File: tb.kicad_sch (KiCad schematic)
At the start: 67 parts, among them U4 JHL6340SLLSQ, U5 MX25L8006EM1I-12G, U6 SI52112-B6-GT, U7 MX25L8006EM2I-12G, Y1 ABM8G-25.000MHZ-B4Y-T, Y2 ABM8G-25.000MHZ-B4Y-T

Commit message: [#58582] Globlib
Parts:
- C100, C102, C103, C105, C106, C107, C108, C109, C110, C111, C112, C99: footprint thunderbolt-pcie-adapter-footprints:C_0402_1005Metric -> antmicro-footprints:C_0402_1005Metric; symbol thunderbolt-pcie-adapter:C_220n_0402 -> antmicroCapacitors0402:C_220n_0402
- C101, C104, C115, C98: footprint thunderbolt-pcie-adapter-footprints:C_0402_1005Metric -> antmicro-footprints:C_0402_1005Metric; symbol thunderbolt-pcie-adapter:C_100n_0402 -> antmicroCapacitors0402:C_100n_0402
- C113, C114, C116, C117: footprint thunderbolt-pcie-adapter-footprints:C_0402_1005Metric -> antmicro-footprints:C_0402_1005Metric; symbol thunderbolt-pcie-adapter:C_10p_0402 -> antmicroCapacitors0402:C_10p_0402
- R50, R51, R52, R53: footprint thunderbolt-pcie-adapter-footprints:R_0402_1005Metric -> antmicro-footprints:R_0402_1005Metric; symbol thunderbolt-pcie-adapter:R_3k3_0402 -> antmicroResistors0402:R_3k3_0402
- R54, R55, R70, R71, R82: footprint thunderbolt-pcie-adapter-footprints:R_0402_1005Metric -> antmicro-footprints:R_0402_1005Metric; symbol thunderbolt-pcie-adapter:R_1M_0402 -> antmicroResistors0402:R_1M_0402
- R56, R64, R65, R66, R67, R78, R79, R80, R83, R85: footprint thunderbolt-pcie-adapter-footprints:R_0402_1005Metric -> antmicro-footprints:R_0402_1005Metric; symbol thunderbolt-pcie-adapter:R_10k_0402 -> antmicroResistors0402:R_10k_0402
- R57, R60, R72, R75, R77, R81, R84, R86, R87, R90: footprint thunderbolt-pcie-adapter-footprints:R_0402_1005Metric -> antmicro-footprints:R_0402_1005Metric; symbol thunderbolt-pcie-adapter:R_100k_0402 -> antmicroResistors0402:R_100k_0402
- R58, R59, R61, R62: footprint thunderbolt-pcie-adapter-footprints:R_0402_1005Metric -> antmicro-footprints:R_0402_1005Metric; symbol thunderbolt-pcie-adapter:R_2k2_0402 -> antmicroResistors0402:R_2k2_0402
- R63, R76: footprint thunderbolt-pcie-adapter-footprints:R_0402_1005Metric -> antmicro-footprints:R_0402_1005Metric; symbol thunderbolt-pcie-adapter:R_14k_0402 -> antmicroResistors0402:R_14k_0402
- R68, R73: footprint thunderbolt-pcie-adapter-footprints:R_0402_1005Metric -> antmicro-footprints:R_0402_1005Metric; symbol thunderbolt-pcie-adapter:R_499R_0402 -> antmicroResistors0402:R_499R_0402
- R69: footprint thunderbolt-pcie-adapter-footprints:R_0402_1005Metric -> antmicro-footprints:R_0402_1005Metric; symbol thunderbolt-pcie-adapter:R_4k75_0.5%_0402 -> antmicroResistors0402:R_4k75_0.5%_0402
- R74: footprint thunderbolt-pcie-adapter-footprints:R_0402_1005Metric -> antmicro-footprints:R_0402_1005Metric; symbol thunderbolt-pcie-adapter:R_3k01_0402 -> antmicroResistors0402:R_3k01_0402
- R88, R89: footprint thunderbolt-pcie-adapter-footprints:R_0402_1005Metric -> antmicro-footprints:R_0402_1005Metric; symbol thunderbolt-pcie-adapter:R_100R_0402 -> antmicroResistors0402:R_100R_0402
- U4: footprint thunderbolt-pcie-adapter-footprints:JHL6340SLLSQ -> antmicro-footprints:JHL6340SLLSQ; symbol thunderbolt-pcie-adapter:JHL6340SLLSQ -> antmicroInterfaceControllers:JHL6340SLLSQ
- U5: footprint thunderbolt-pcie-adapter-footprints:SOIC-8_3.9x4.9x1.75mm_P1.27mm -> antmicro-footprints:SOIC-8_3.9x4.9x1.75mm_P1.27mm; symbol thunderbolt-pcie-adapter:MX25L8006EM1I-12G -> antmicroMemory:MX25L8006EM1I-12G
- U6: footprint thunderbolt-pcie-adapter-footprints:TSSOP-8_3x4.4mm_P0.65mm -> antmicro-footprints:TSSOP-8_3x4.4mm_P0.65mm; symbol thunderbolt-pcie-adapter:SI52112-B6-GT -> antmicroClockTimingClockGeneratorsPLLsFrequencySynthesizers:SI52112-B6-GT
- U7: footprint thunderbolt-pcie-adapter-footprints:SOIC-8_5.3x5.3x2mm_P1.27mm -> antmicro-footprints:SOIC-8_5.3x5.3x2mm_P1.27mm; symbol thunderbolt-pcie-adapter:MX25L8006EM2I-12G -> antmicroMemory:MX25L8006EM2I-12G

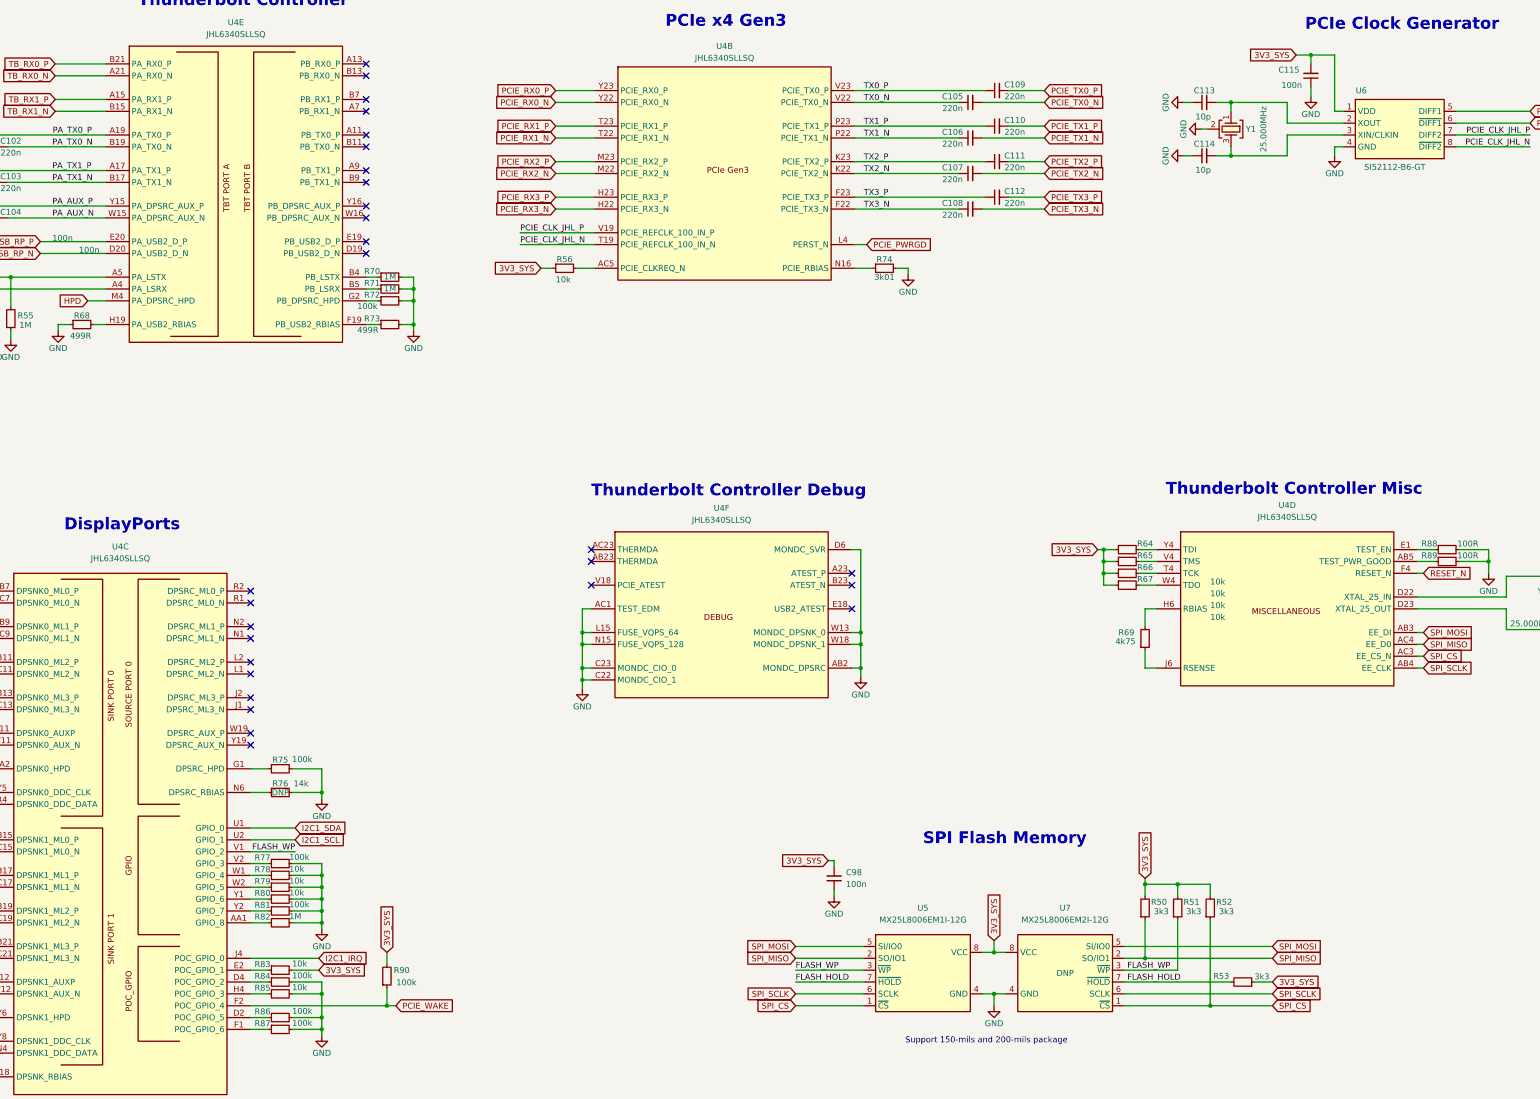
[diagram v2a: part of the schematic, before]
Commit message: [#58582] Update ICs to global libs
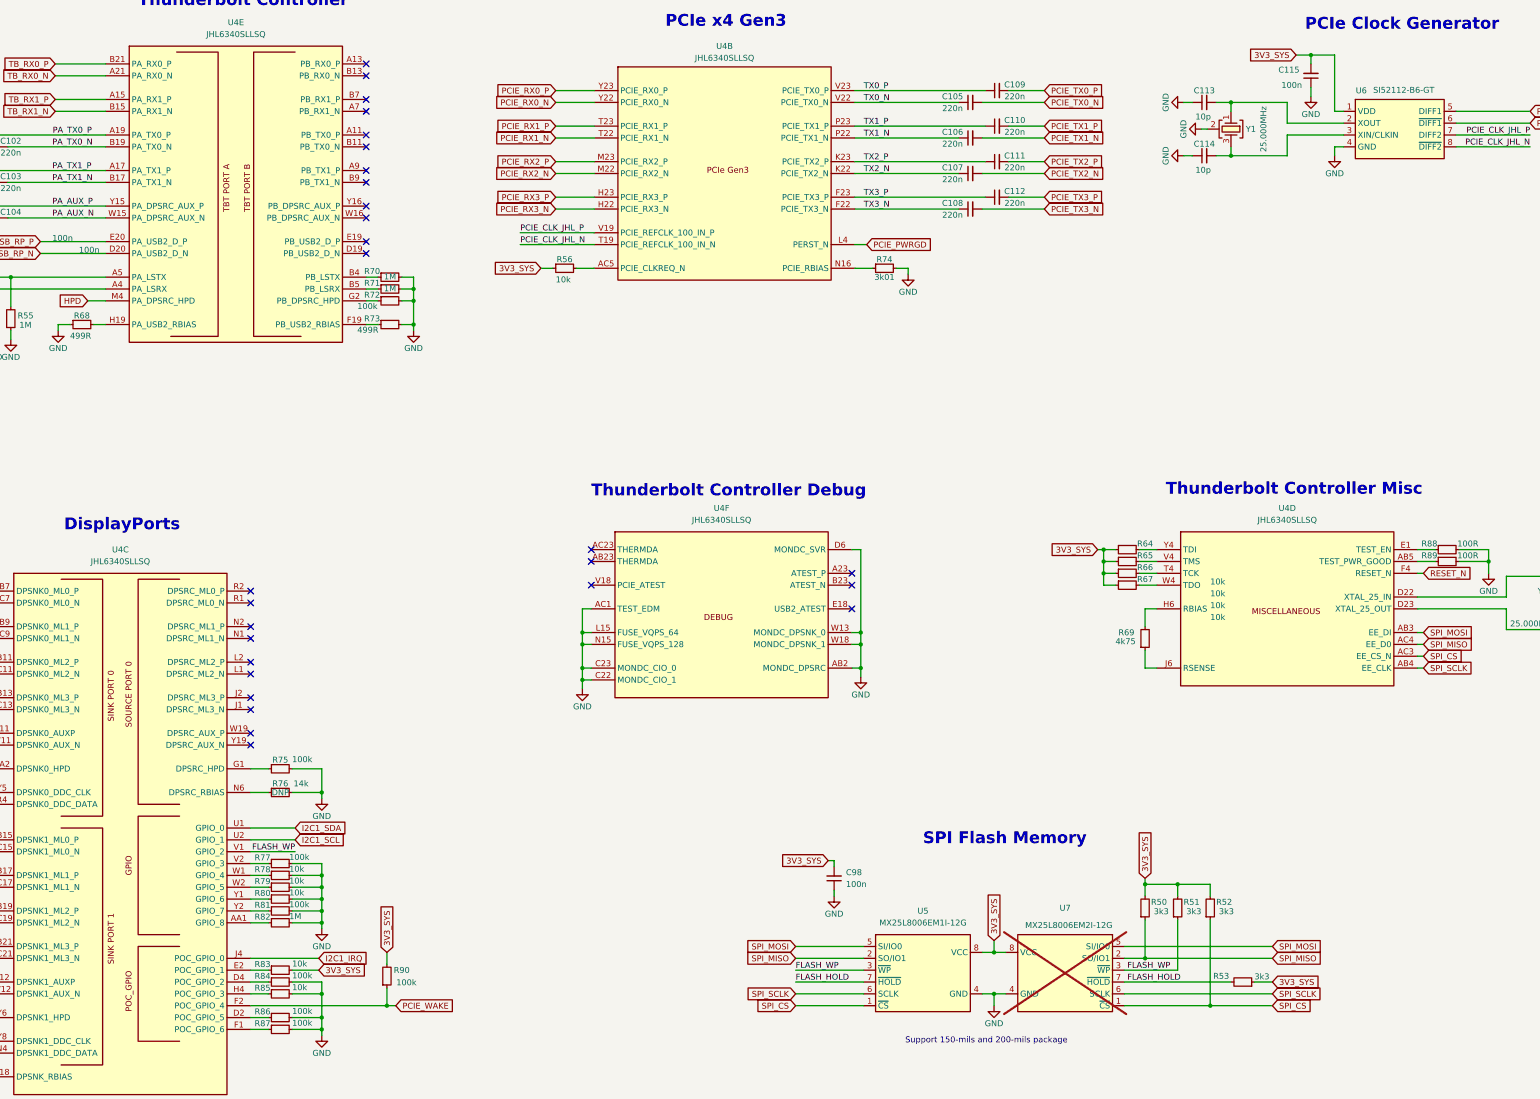
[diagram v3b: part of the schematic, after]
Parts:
- U6: Manufacturer Skyworks -> Skyworks Solutions
- U7: DNP DNP -> (none); now not fitted
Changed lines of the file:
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@@
     )
   )
-  (symbol (lib_name "JHL6340SLLSQ_3") (lib_id "antmicroInterfaceControllers:JHL6340SLLSQ") (at 76.2 40.64 0) (unit 5)
+  (symbol (lib_id "antmicroInterfaceControllers:JHL6340SLLSQ") (at 76.2 40.64 0) (unit 5)
     (in_bom yes) (on_board yes) (dnp no) (fields_autoplaced)
     (property "Reference" "U4" (at 104.14 31.75 0)
@@
   )
   (symbol (lib_id "antmicroMemory:MX25L8006EM2I-12G") (at 294.64 229.87 0) (mirror y) (unit 1)
-    (in_bom yes) (on_board yes) (dnp no)
+    (in_bom yes) (on_board yes) (dnp yes)
     (property "Reference" "U7" (at 281.94 221.615 0)
       (effects (font (size 1.27 1.27) (thickness 0.15)))
     )
-    (property "Value" "MX25L8006EM2I-12G" (at 281.94 224.155 0)
-      (effects (font (size 1.27 1.27) (thickness 0.15)))
+    (property "Value" "MX25L8006EM2I-12G" (at 292.1 226.06 0)
+      (effects (font (size 1.27 1.27) (thickness 0.15)) (justify left bottom))
     )
     (property "Footprint" "antmicro-footprints:SOIC-8_5.3x5.3x2mm_P1.27mm" (at 259.08 234.95 0)
@@
       (effects (font (size 1.27 1.27) (thickness 0.15)) (justify left bottom) hide)
     )
-    (property "DNP" "DNP" (at 281.94 235.585 0)
-      (effects (font (size 1.27 1.27)))
-    )
     (pin "1")
     (pin "2")
@@
   (symbol (lib_id "antmicroMemory:MX25L8006EM1I-12G") (at 238.76 229.87 0) (unit 1)
     (in_bom yes) (on_board yes) (dnp no) (fields_autoplaced)
-    (property "Reference" "U5" (at 251.46 221.615 0)
+    (property "Reference" "U5" (at 251.46 222.25 0)
       (effects (font (size 1.27 1.27) (thickness 0.15)))
     )
-    (property "Value" "MX25L8006EM1I-12G" (at 251.46 224.155 0)
+    (property "Value" "MX25L8006EM1I-12G" (at 251.46 224.79 0)
       (effects (font (size 1.27 1.27) (thickness 0.15)))
     )
@@
       (effects (font (size 1.27 1.27) (thickness 0.15)))
     )
-    (property "Value" "SI52112-B6-GT" (at 346.075 63.5 0)
+    (property "Value" "SI52112-B6-GT" (at 347.98 46.99 0)
       (effects (font (size 1.27 1.27) (thickness 0.15)) (justify left bottom))
     )
@@
       (effects (font (size 1.27 1.27) (thickness 0.15)) (justify left bottom) hide)
     )
-    (property "Manufacturer" "Skyworks" (at 379.73 66.04 0)
+    (property "Manufacturer" "Skyworks Solutions" (at 379.73 66.04 0)
       (effects (font (size 1.27 1.27) (thickness 0.15)) (justify left bottom) hide)
     )
@@
     )
   )
-  (symbol (lib_name "JHL6340SLLSQ_4") (lib_id "antmicroInterfaceControllers:JHL6340SLLSQ") (at 51.435 153.67 0) (unit 3)
+  (symbol (lib_id "antmicroInterfaceControllers:JHL6340SLLSQ") (at 51.435 153.67 0) (unit 3)
     (in_bom yes) (on_board yes) (dnp no) (fields_autoplaced)
-    (property "Reference" "U4" (at 79.375 144.145 0)
+    (property "Reference" "U4" (at 79.375 144.78 0)
       (effects (font (size 1.27 1.27) (thickness 0.15)))
     )
-    (property "Value" "JHL6340SLLSQ" (at 79.375 146.685 0)
+    (property "Value" "JHL6340SLLSQ" (at 79.375 147.32 0)
       (effects (font (size 1.27 1.27) (thickness 0.15)))
     )
@@
     )
   )
-  (symbol (lib_name "JHL6340SLLSQ_2") (lib_id "antmicroInterfaceControllers:JHL6340SLLSQ") (at 180.34 144.78 0) (unit 6)
+  (symbol (lib_id "antmicroInterfaceControllers:JHL6340SLLSQ") (at 180.34 144.78 0) (unit 6)
     (in_bom yes) (on_board yes) (dnp no) (fields_autoplaced)
     (property "Reference" "U4" (at 208.28 135.89 0)
@@
     )
   )
-  (symbol (lib_name "JHL6340SLLSQ_1") (lib_id "antmicroInterfaceControllers:JHL6340SLLSQ") (at 301.625 144.78 0) (unit 4)
+  (symbol (lib_id "antmicroInterfaceControllers:JHL6340SLLSQ") (at 301.625 144.78 0) (unit 4)
     (in_bom yes) (on_board yes) (dnp no) (fields_autoplaced)
-    (property "Reference" "U4" (at 329.565 135.255 0)
+    (property "Reference" "U4" (at 329.565 135.89 0)
       (effects (font (size 1.27 1.27) (thickness 0.15)))
     )
-    (property "Value" "JHL6340SLLSQ" (at 329.565 137.795 0)
+    (property "Value" "JHL6340SLLSQ" (at 329.565 138.43 0)
       (effects (font (size 1.27 1.27) (thickness 0.15)))
     )

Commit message: [#58582] Update GND to global
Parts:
- removed Y1, Y2: ABM8G-25.000MHZ-B4Y-T, thunderbolt-pcie-adapter-footprints:Oscillator_SMD_Geyer_KX-7-4Pin_3.2x2.5mm, symbol thunderbolt-pcie-adapter:ABM8G-25.000MHZ-B4Y-T
- added Y1, Y2: Resonator_25MHz_ABM8G, antmicro-footprints:Resonator_SMD_Abracon_ABM8G_3.2x2.5mm, symbol antmicroResonators:Resonator_25MHz_ABM8G
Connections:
- net GND: now also Y1.2 (SH), Y1.4 (SH), Y2.2 (SH), Y2.4 (SH)
- net at C113.2, U6.2 (XOUT): now also Y1.1
- net at C114.2, U6.3 (XIN/CLKIN): now also Y1.3
- net at C117.1, U4.D23 (XTAL_25_OUT): now also Y2.1
- net at C116.1, U4.D22 (XTAL_25_IN): now also Y2.3

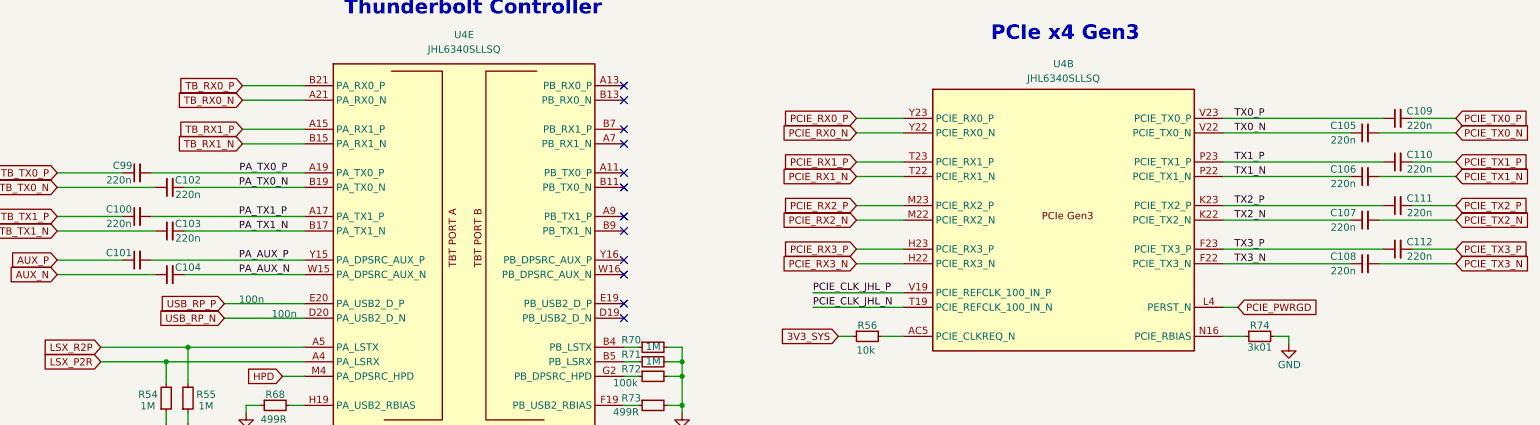
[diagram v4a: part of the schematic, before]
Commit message: [#58582] Clean ERC
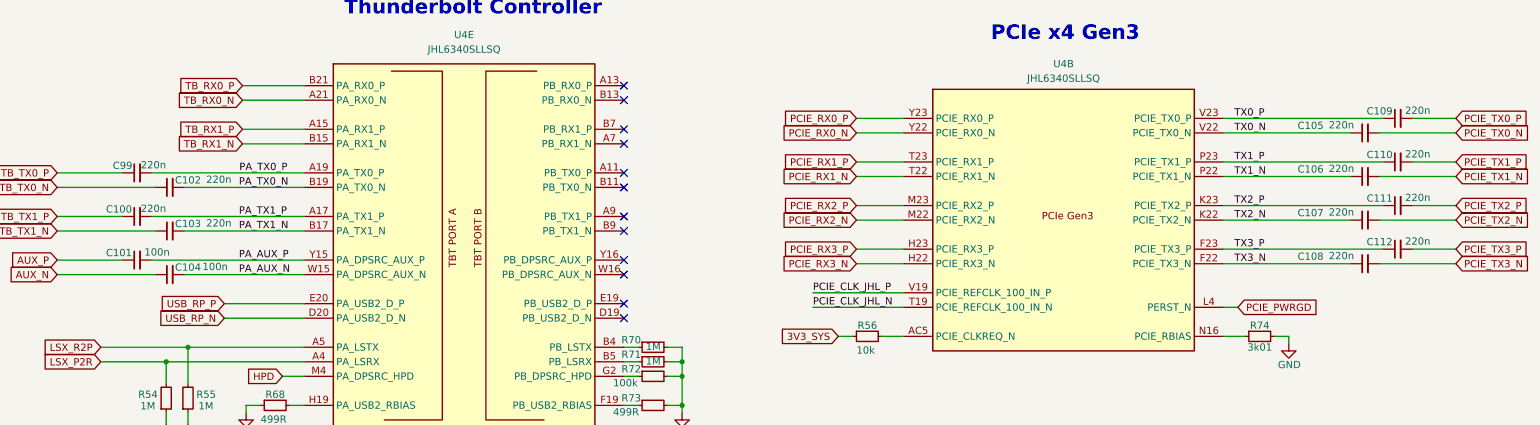
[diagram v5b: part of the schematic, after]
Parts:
- C100, C102, C103, C105, C106, C107, C108, C109, C110, C111, C112, C99: Manufacturer Yaego -> YAGEO
- U7: now left out of the parts list

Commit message: [#58582] Update symbols values visibility
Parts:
- R63, R76: now not fitted; now left out of the parts list
- R68, R73: Manufacturer Vishay -> Bourns
- U7: DNP (none) -> DNP
